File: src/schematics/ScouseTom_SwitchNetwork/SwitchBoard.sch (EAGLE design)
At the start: 47 parts, among them U1 ADUM1410ARWZ, U2 MCP73831, X1 DSUB _T, X2 DSUB_B, X3 USB-MICROB

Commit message: Added Mak Connector for Silicon Elec to Schematics. Started routing Switchboard
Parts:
- added C11, C12, C13, C14, C15, C18, C5, C6, C7, C8: 0.1uF, resistor:C-EUC0805
- added DSUB3: CTR_IN, con-subd:F09HP
- added JP3, JP4: (no value), pinhead:PINHD-1X2
- added JP5: (no value), pinhead:PINHD-2X9
- DSUB1: value (none) -> CTR_OUT
- DSUB2: value CTR_DSUB -> CTR_ARD
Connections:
- new net DIN+_DCHN: DSUB3.3, JP5.10
- new net DIN-_DCHN: DSUB3.7, JP5.8
- new net GND_DCHN: DSUB3.6, JP5.4
- new net N$10: DSUB1.G1, DSUB1.G2, JP3.2
- new net N$12: DSUB3.G1, DSUB3.G2, JP4.1
- new net RESET: DSUB1.8, JP5.11
- new net RESET_DCHN: DSUB3.8, JP5.12
- new net SCLK_DCHN: DSUB3.2, JP5.6
- new net SYNC: DSUB1.4, JP5.13
- new net SYNC_DCHN: DSUB3.4, JP5.14
- new net TEST_1_DCHN: DSUB3.5, JP5.18
- new net TEST_2_DCHN: DSUB3.1, JP5.2
- new net VDD_DCHN: DSUB3.9, JP5.16
- net AGND: now also C11.1, C12.1, C13.1, C14.1, C15.1, C18.1, C5.1, C6.1, C7.1, C8.1, DSUB1.6, JP3.1, JP4.2, JP5.3
- net DIN+: now also DSUB1.3, JP5.9
- net DIN-: now also DSUB1.7, JP5.7
- net SCLK: now also DSUB1.2, JP5.5
- net TEST_1: now also DSUB1.5, JP5.17
- net TEST_2: now also DSUB1.1, JP5.1
- net VDD: now also C11.2, C12.2, C13.2, C14.2, C15.2, C18.2, C5.2, C6.2, C7.2, C8.2, DSUB1.9, JP5.15
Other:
- note added: "DSUB FROM ARDUINO"
- note added: "DSUB TO NEXT SWITCH FOR DAISY CHAIN"
- note added: "Jumper to connect shield to AGND"
- note removed: "DSUB TO SWITCH NETWORK"
- moved on the sheet: JP1

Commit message: SwNet - left hand side layout done
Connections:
- net N$1 renamed DIN+2
- net N$2 renamed DIN+4
- net N$3 renamed DIN+3
- net N$4 renamed DIN-2
- net N$5 renamed DIN+5
- net N$6 renamed DIN-3
- net N$7 renamed DIN-4
- net N$8 renamed DIN-5
- removed net RESET: DSUB1.8, JP5.11
- removed net SYNC: DSUB1.4, JP5.13
- net DIN+: no longer DSUB1.3
- net DIN-: no longer DSUB1.7
- net DOUT+: now also DSUB1.3
- net DOUT-: now also DSUB1.7
- net ~RESET: now also DSUB1.8, JP5.11
- net ~SYNC: now also DSUB1.4, JP5.13

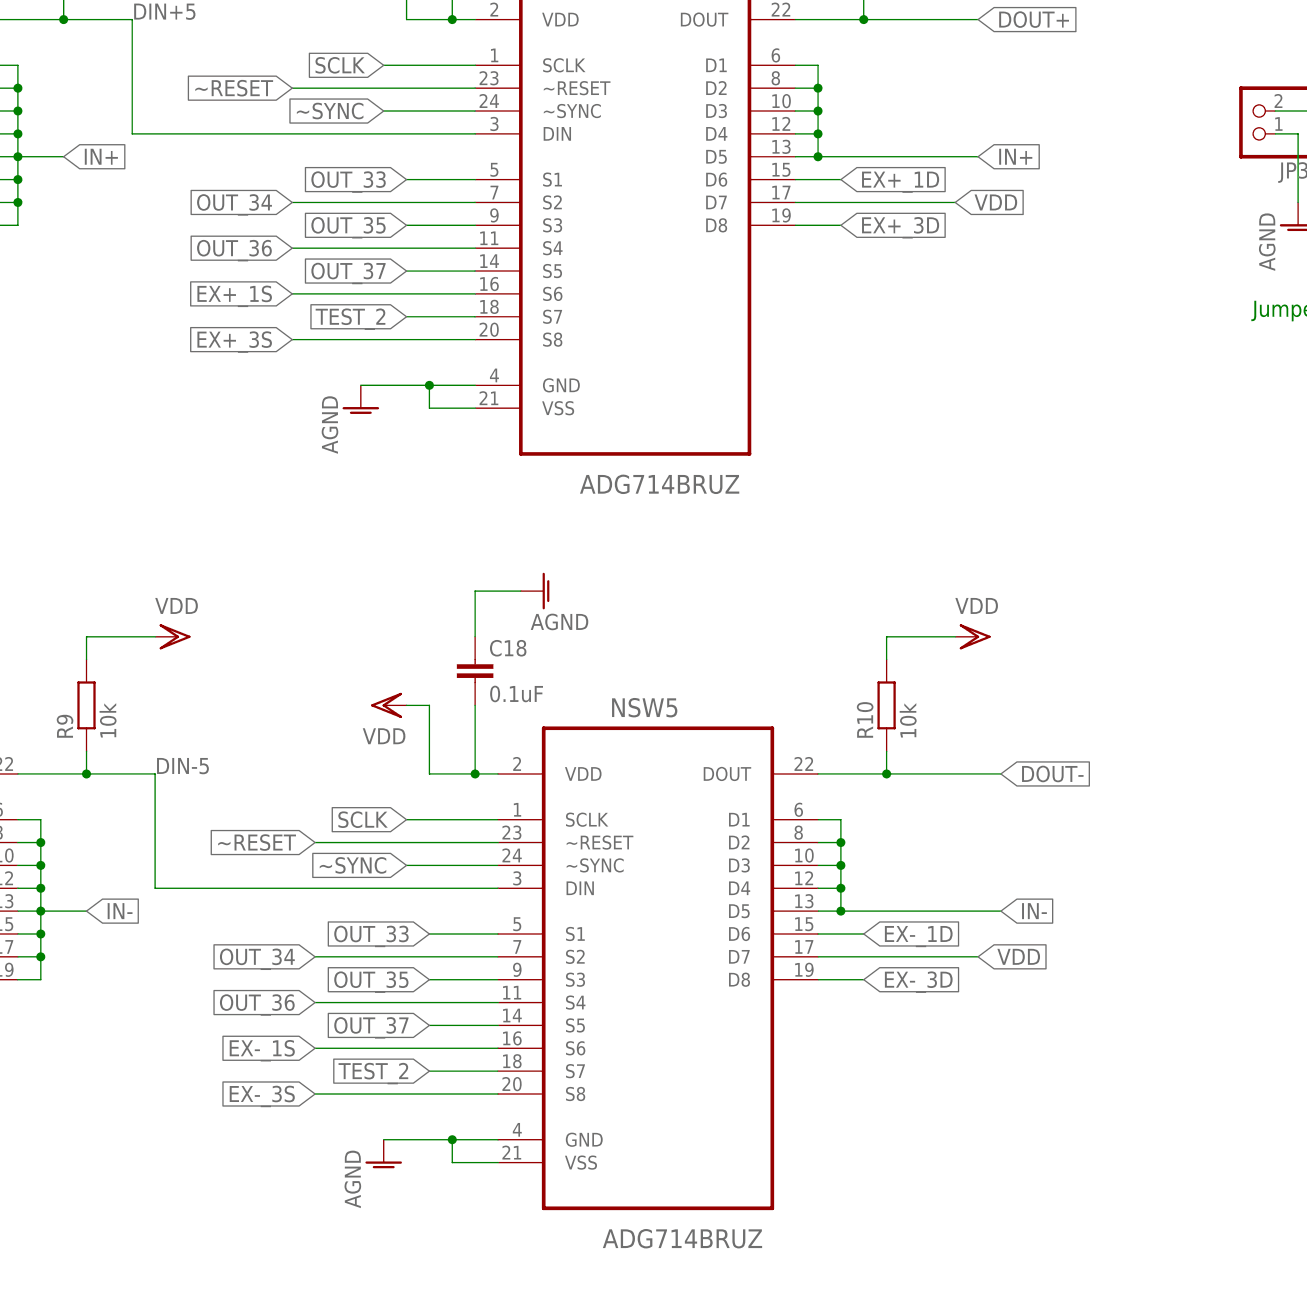
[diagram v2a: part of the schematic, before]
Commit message: SwitchBoard Switches routed
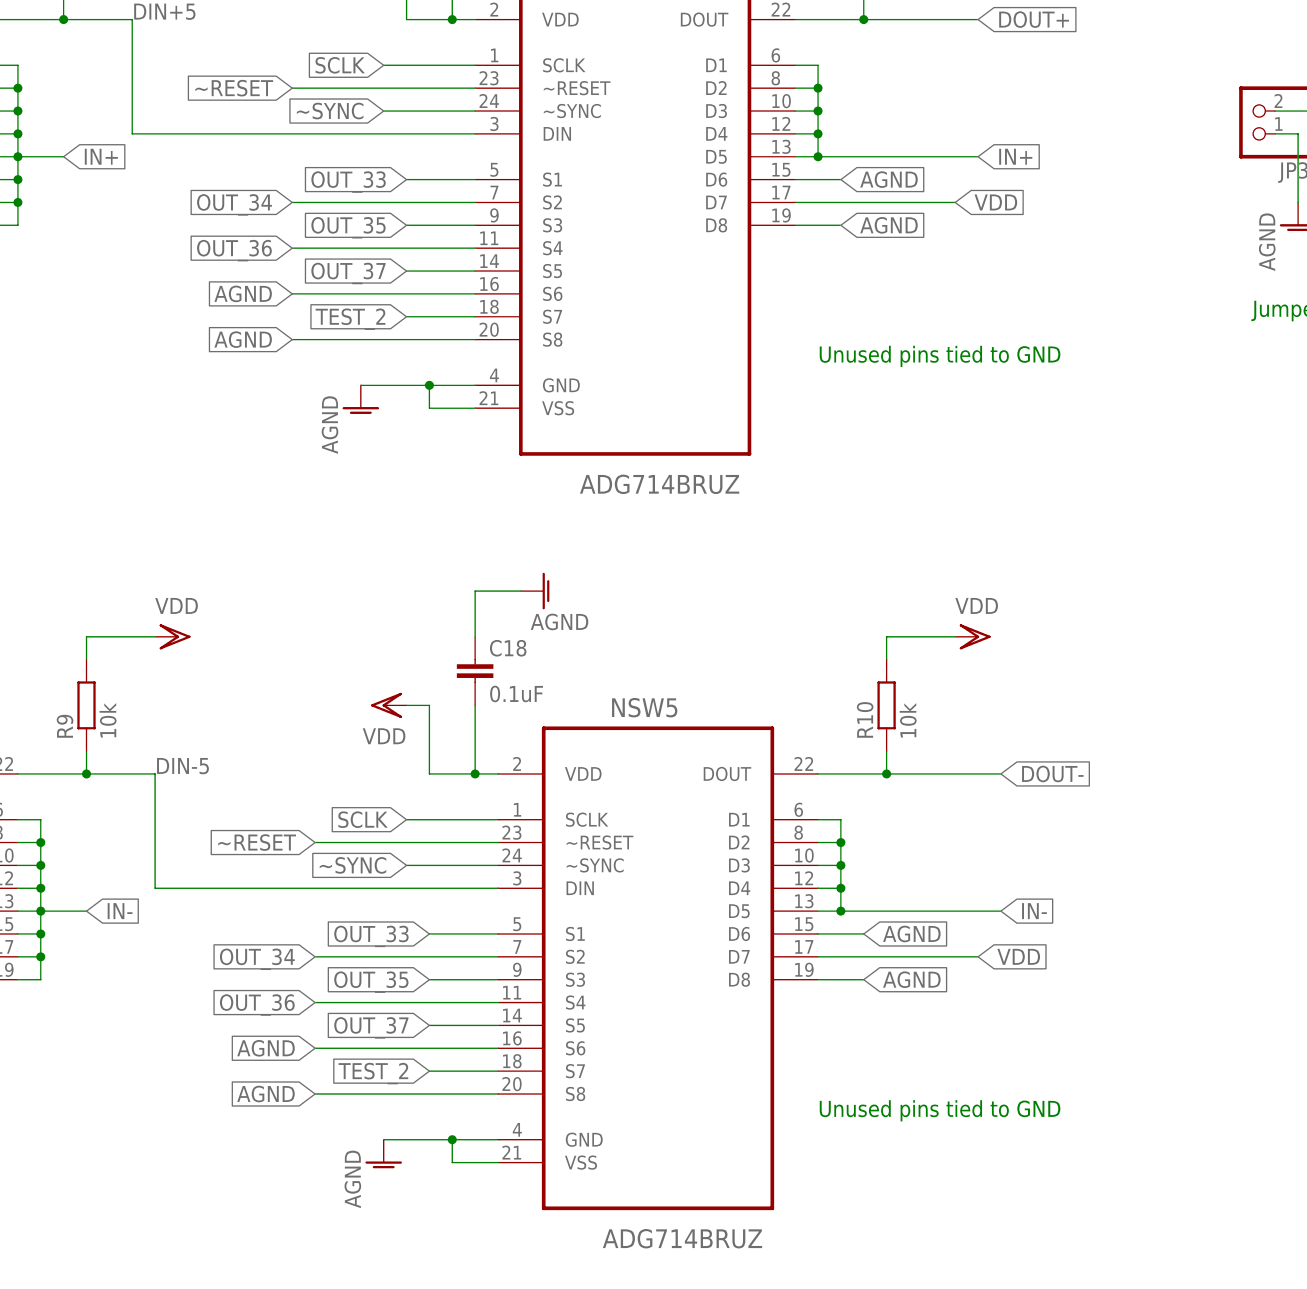
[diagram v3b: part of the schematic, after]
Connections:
- removed net EX+_1D: PSW5.D6
- removed net EX+_1S: PSW5.S6
- removed net EX+_3D: PSW5.D8
- removed net EX+_3S: PSW5.S8
- removed net EX-_1D: NSW5.D6
- removed net EX-_1S: NSW5.S6
- removed net EX-_3D: NSW5.D8
- removed net EX-_3S: NSW5.S8
- net AGND: now also NSW5.D6, NSW5.D8, NSW5.S6, NSW5.S8, PSW5.D6, PSW5.D8, PSW5.S6, PSW5.S8
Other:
- note added: "Unused pins tied to GND"
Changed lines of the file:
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@@
 <text x="91.44" y="88.9" size="1.778" layer="91">Jumper to connect shield to AGND</text>
 <text x="139.7" y="116.84" size="1.778" layer="91">DSUB TO NEXT SWITCH FOR DAISY CHAIN</text>
+<text x="43.18" y="83.82" size="1.778" layer="91">Unused pins tied to GND</text>
+<text x="43.18" y="0" size="1.778" layer="91">Unused pins tied to GND</text>
 </plain>
 <instances>
@@
 <pinref part="AGND37" gate="VR1" pin="AGND"/>
 </segment>
+<segment>
+<pinref part="PSW5" gate="A" pin="D6"/>
+<wire x1="40.64" y1="104.14" x2="45.72" y2="104.14" width="0.1524" layer="91"/>
+<label x="45.72" y="104.14" size="1.778" layer="95" xref="yes"/>
+</segment>
+<segment>
+<pinref part="PSW5" gate="A" pin="D8"/>
+<wire x1="40.64" y1="99.06" x2="45.72" y2="99.06" width="0.1524" layer="91"/>
+<label x="45.72" y="99.06" size="1.778" layer="95" xref="yes"/>
+</segment>
+<segment>
+<pinref part="PSW5" gate="A" pin="S6"/>
+<wire x1="5.08" y1="91.44" x2="-15.24" y2="91.44" width="0.1524" layer="91"/>
+<label x="-15.24" y="91.44" size="1.778" layer="95" rot="R180" xref="yes"/>
+</segment>
+<segment>
+<pinref part="PSW5" gate="A" pin="S8"/>
+<wire x1="5.08" y1="86.36" x2="-15.24" y2="86.36" width="0.1524" layer="91"/>
+<label x="-15.24" y="86.36" size="1.778" layer="95" rot="R180" xref="yes"/>
+</segment>
+<segment>
+<pinref part="NSW5" gate="A" pin="D6"/>
+<wire x1="43.18" y1="20.32" x2="48.26" y2="20.32" width="0.1524" layer="91"/>
+<label x="48.26" y="20.32" size="1.778" layer="95" xref="yes"/>
+</segment>
+<segment>
+<pinref part="NSW5" gate="A" pin="D8"/>
+<wire x1="43.18" y1="15.24" x2="48.26" y2="15.24" width="0.1524" layer="91"/>
+<label x="48.26" y="15.24" size="1.778" layer="95" xref="yes"/>
+</segment>
+<segment>
+<pinref part="NSW5" gate="A" pin="S6"/>
+<wire x1="7.62" y1="7.62" x2="-12.7" y2="7.62" width="0.1524" layer="91"/>
+<label x="-12.7" y="7.62" size="1.778" layer="95" rot="R180" xref="yes"/>
+</segment>
+<segment>
+<pinref part="NSW5" gate="A" pin="S8"/>
+<wire x1="7.62" y1="2.54" x2="-12.7" y2="2.54" width="0.1524" layer="91"/>
+<label x="-12.7" y="2.54" size="1.778" layer="95" rot="R180" xref="yes"/>
+</segment>
 </net>
 <net name="VDD" class="0">
@@
 </segment>
 </net>
-<net name="EX+_1S" class="0">
-<segment>
-<pinref part="PSW5" gate="A" pin="S6"/>
-<wire x1="5.08" y1="91.44" x2="-15.24" y2="91.44" width="0.1524" layer="91"/>
-<label x="-15.24" y="91.44" size="1.778" layer="95" rot="R180" xref="yes"/>
-</segment>
-</net>
-<net name="EX+_3S" class="0">
-<segment>
-<pinref part="PSW5" gate="A" pin="S8"/>
-<wire x1="5.08" y1="86.36" x2="-15.24" y2="86.36" width="0.1524" layer="91"/>
-<label x="-15.24" y="86.36" size="1.778" layer="95" rot="R180" xref="yes"/>
-</segment>
-</net>
-<net name="EX+_1D" class="0">
-<segment>
-<pinref part="PSW5" gate="A" pin="D6"/>
-<wire x1="40.64" y1="104.14" x2="45.72" y2="104.14" width="0.1524" layer="91"/>
-<label x="45.72" y="104.14" size="1.778" layer="95" xref="yes"/>
-</segment>
-</net>
-<net name="EX+_3D" class="0">
-<segment>
-<pinref part="PSW5" gate="A" pin="D8"/>
-<wire x1="40.64" y1="99.06" x2="45.72" y2="99.06" width="0.1524" layer="91"/>
-<label x="45.72" y="99.06" size="1.778" layer="95" xref="yes"/>
-</segment>
-</net>
 <net name="DIN-2" class="0">
 <segment>
@@
 </segment>
 </net>
-<net name="EX-_1S" class="0">
-<segment>
-<pinref part="NSW5" gate="A" pin="S6"/>
-<wire x1="7.62" y1="7.62" x2="-12.7" y2="7.62" width="0.1524" layer="91"/>
-<label x="-12.7" y="7.62" size="1.778" layer="95" rot="R180" xref="yes"/>
-</segment>
-</net>
-<net name="EX-_3S" class="0">
-<segment>
-<pinref part="NSW5" gate="A" pin="S8"/>
-<wire x1="7.62" y1="2.54" x2="-12.7" y2="2.54" width="0.1524" layer="91"/>
-<label x="-12.7" y="2.54" size="1.778" layer="95" rot="R180" xref="yes"/>
-</segment>
-</net>
 <net name="DOUT-" class="0">
 <segment>
@@
 </segment>
 </net>
-<net name="EX-_1D" class="0">
-<segment>
-<pinref part="NSW5" gate="A" pin="D6"/>
-<wire x1="43.18" y1="20.32" x2="48.26" y2="20.32" width="0.1524" layer="91"/>
-<label x="48.26" y="20.32" size="1.778" layer="95" xref="yes"/>
-</segment>
-</net>
-<net name="EX-_3D" class="0">
-<segment>
-<pinref part="NSW5" gate="A" pin="D8"/>
-<wire x1="43.18" y1="15.24" x2="48.26" y2="15.24" width="0.1524" layer="91"/>
-<label x="48.26" y="15.24" size="1.778" layer="95" xref="yes"/>
-</segment>
-</net>

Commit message: Switch Board Layout finished, needs text and logo
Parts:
- removed D4: red, SparkFun:LED0603
- added C21, C24, C25: 10uF, resistor:C-EUC0805
- added C22, C26: 100uF, rcl:CPOL-EUCT6032
- added C23: 0.01uF, resistor:C-EUC0805
- added C28: 2.2uF, resistor:C-EUC0805
- added CHRG: YELLOW, led:LEDSML0805
- added FULL, LBO, PWR: GREEN, led:LEDSML0805
- added IC2: LT1763CDE-5, linear-technology:LT1763CDE-5
- added L2: 6.8uH, WE-PD:WE-PD-7447779006_7332/7345_PLASTIC_BASE
- added ON/OFF: (no value), pinhead:PINHD-1X2
- added R15: 2k, rcl:R-EU_M0805
- added R16: 1.8M, rcl:R-EU_M0805
- added R17, R21: 1k, rcl:R-EU_M0805
- added R18: 200k, rcl:R-EU_M0805
- added R19: 82k, rcl:R-EU_M0805
- added R20: 2M, rcl:R-EU_M0805
- added R22: 4.7k, rcl:R-EU_M0805
- added R23: 360k, rcl:R-EU_M0805
- added R24: 47k, rcl:R-EU_M0805
- added T1: (no value), transistor:BC807-40-PNP-SOT23-BEC
- added U3: TPS61090RSAR, Adafruit PowerBoost 500C:VREG_TPS6103XSPARKFUNVERSION
- C10: value 4.7uF -> 10uF; device SparkFun:CAP0402-CAP -> resistor:C-EUC0805
- C9: value 4.7uF -> 0.1uF; device SparkFun:CAP0402-CAP -> resistor:C-EUC0805
- R13: value 470 -> 1k; device SparkFun:RESISTOR0402-RES -> rcl:R-EU_M0805
- R14: value 2k -> 470; device SparkFun:RESISTOR0402-RES -> rcl:R-EU_M0805
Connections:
- removed net N$14: R13.1, U2.STAT
- removed net N$17: JP12.2, JP2.1
- removed net VBATT: C10.1, JP12.1, JP2.2, U2.VBAT
- new net LBO: R22.1, U3.LBO
- new net LB_REF: R20.1, R23.2, U3.LBI
- new net N$2: CHRG.C, R14.2
- new net N$3: C23.1, IC2.OUT@2, IC2.SENSE
- new net N$4: C23.2, IC2.BYP
- new net N$5: FULL.A, R13.2
- new net N$6: R16.1, R19.2
- new net N$7: PWR.C, R17.1
- new net N$8: R21.1, T1.C
- new net PROG: R15.2, U2.PROG
- new net STAT: R13.1, R14.1, U2.STAT
- new net SW: L2.2, U3.SW
- new net VBATT_A: C24.1, JP12.1, JP2.2, ON/OFF.1, U2.VBAT
- new net VBATT_B: C25.1, C9.1, L2.1, ON/OFF.2, R20.2, R24.2, T1.E, U3.EN, U3.VBAT
- new net VREG: C21.1, C26.+, C28.1, IC2.!SHDN, IC2.IN@1, IC2.IN@2, PWR.A, R16.2, U3.VOUT
- new net VSET: R18.2, R19.1, U3.FB
- net 5VIN: now also C10.1, CHRG.A; no longer C9.1, D4.A
- net AGND: now also C21.2, C22.-, C24.2, C25.2, C26.-, C28.2, FULL.C, IC2.EXP, IC2.GND, JP12.2, JP2.1, LBO.C, R15.1, R17.2, R18.1, R23.1, U3.GND, U3.PGND, U3.SYNC; no longer R14.2
- net DIN+: now also JP5.7; no longer JP5.9
- net DIN+_DCHN: now also JP5.8; no longer JP5.10
- net DIN-: now also JP5.9; no longer JP5.7
- net DIN-_DCHN: now also JP5.10; no longer JP5.8
- net GND: now also U$1.GND1, U$1.GND1_2
- net N$11: now also R22.2, R24.1, T1.B; no longer R14.1, U2.PROG
- net N$9: now also LBO.A, R21.2; no longer D4.C, R13.2
- net RESET_DCHN: now also JP5.14; no longer JP5.12
- net SCLK: now also JP5.11; no longer JP5.5
- net SCLK_DCHN: now also JP5.12; no longer JP5.6
- net SYNC_DCHN: now also JP5.6; no longer JP5.14
- net TEST_1: now also JP5.15; no longer JP5.17
- net TEST_1_DCHN: now also JP5.16; no longer JP5.18
- net TEST_2: now also JP5.17; no longer JP5.1
- net TEST_2_DCHN: now also JP5.18; no longer JP5.2
- net VDD: now also C22.+, IC2.OUT@1, JP5.1; no longer JP5.15
- net VDD_DCHN: now also JP5.2; no longer JP5.16
- net ~RESET: now also JP5.13; no longer JP5.11
- net ~SYNC: now also JP5.5; no longer JP5.13
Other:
- note added: "2K R programs for 500mA output"
- note added: "5V LDO REG FOR SMOOTHING"
- note added: "6.8uH power w/2A current"
- note added: "BATT to 5V BUCK BOOST LOW POWER CHECK"
- note added: "BATTERY CHARGER"
- note added: "BATTERY INDICATOR"
- note added: "DISCONNECT BATTERY FROM REGULATORS TO TURN SHIT OFF"
- note added: "NOT CHANGED THIS YET"
- note added: "R2 < 500K R1 = 5.5*R2 (3.2V LBO)"
- note added: "VSET GIVES OUTPUT OF 5.2V 200k must be used so 1.88M needed Split into free components"
- moved on the sheet: C10, C9, JP12, JP2, JP9, U2
